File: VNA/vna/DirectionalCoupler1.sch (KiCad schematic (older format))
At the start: 4 parts, among them T1 1:10, T2 1:10

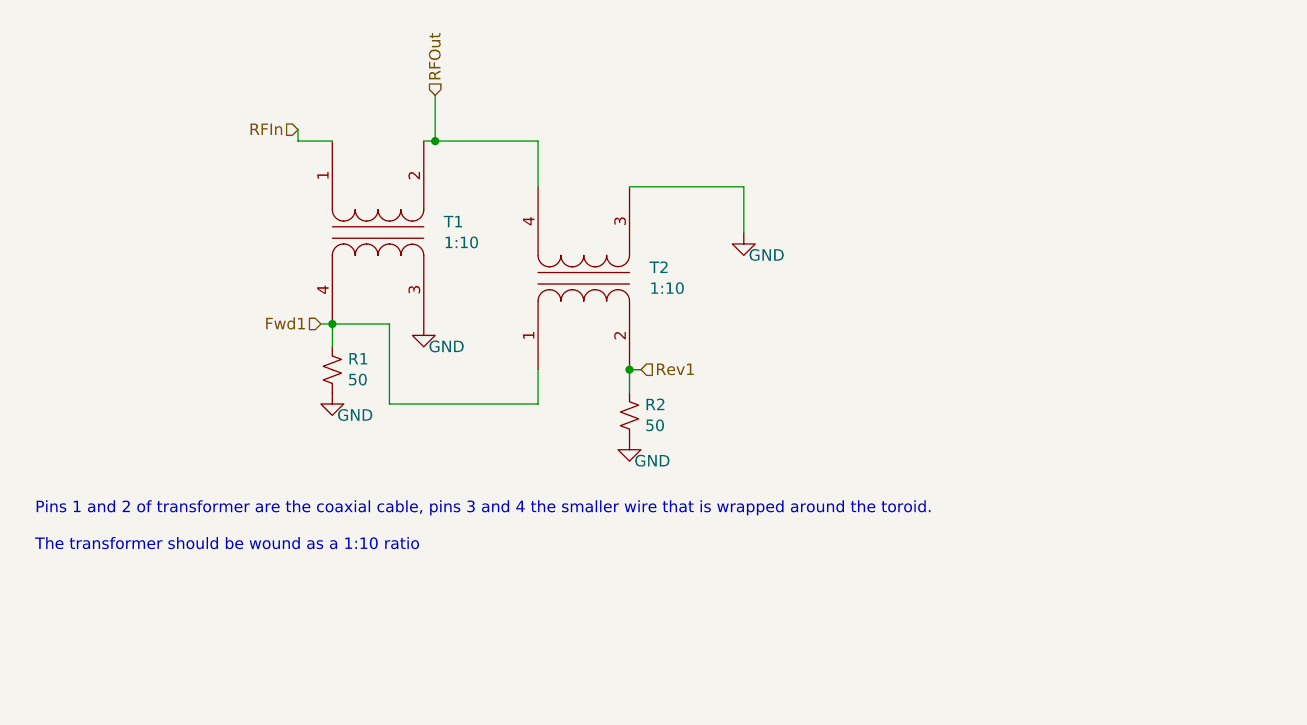
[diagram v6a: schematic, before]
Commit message: custom footprint for couplers, added decoupling caps
added custom footprint for directional couplers - will need to verify it

added decoupling caps to ad9851
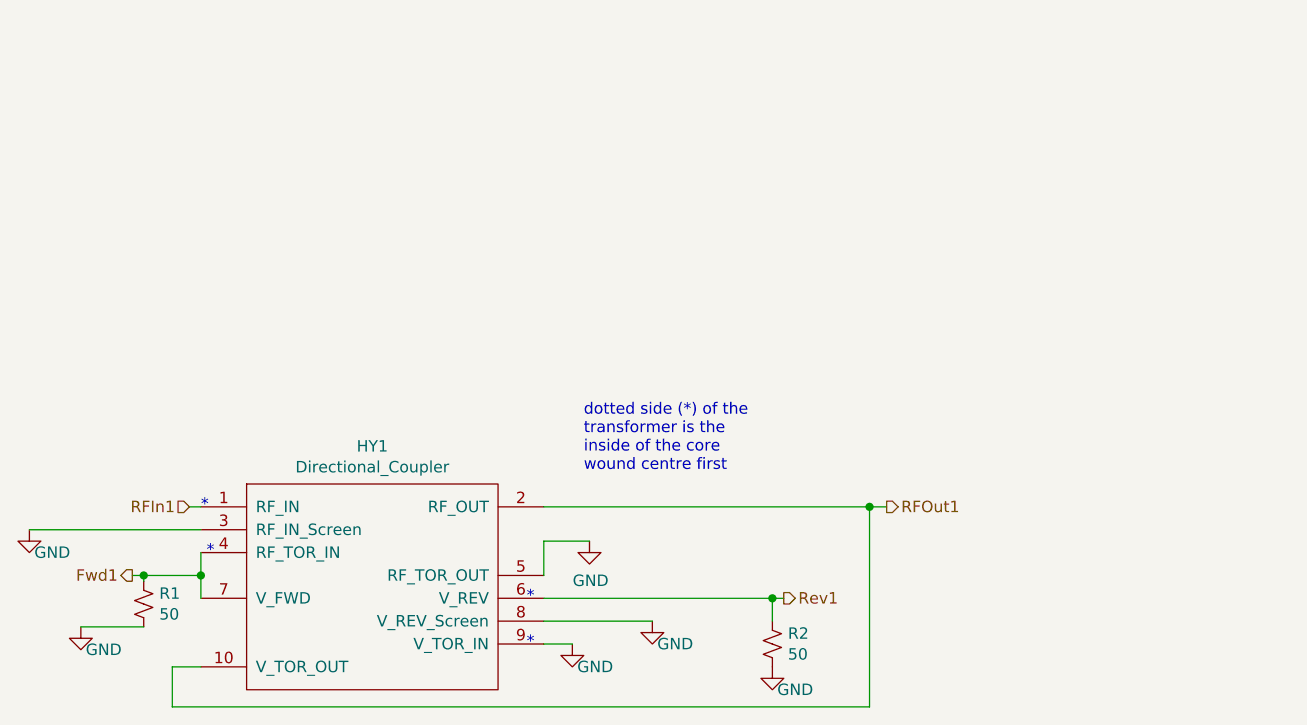
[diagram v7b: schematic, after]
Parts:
- removed T1, T2: 1:10, symbol Device:Transformer_1P_1S
- added HY1: Directional_Coupler, vna:Directional_Coupler, symbol vna-rescue:Directional_Coupler
- R1, R2: footprint Resistor_SMD:R_0805_2012Metric_Pad1.15x1.40mm_HandSolder -> Resistor_SMD:R_1206_3216Metric_Pad1.42x1.75mm_HandSolder
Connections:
- net Fwd1: now also HY1.4 (RF_TOR_IN), HY1.7 (V_FWD)
- net GND: now also HY1.3 (RF_IN_Screen), HY1.5 (RF_TOR_OUT), HY1.8 (V_REV_Screen), HY1.9 (V_TOR_IN)
- net Rev1: now also HY1.6 (V_REV)
- new net RFIn1: HY1.1 (RF_IN)
- new net RFOut1: HY1.10 (V_TOR_OUT), HY1.2 (RF_OUT)
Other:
- note added: "*"
- note added: "dotted side (*) of the \ntransformer is the \ninside of the core\nwound centre first"
- note removed: "Pins 1 and 2 of transformer are the coaxial cable, pins 3 and 4 the smaller wire that is wrapped around the toroid.\n\nThe transformer should be wound as a 1:10 ratio"
- moved on the sheet: R1, R2
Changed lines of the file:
@@
 Comment4 ""
 $EndDescr
-Wire Wire Line
-	6050 2300 6550 2300
-Wire Wire Line
-	6550 2300 6550 2500
 $Comp
 L power:GND #PWR08
 U 1 1 5CF4AF9A
-P 6550 2500
+P 6150 4200
 AR Path="/5CC1CC6B/5CF4AF9A" Ref="#PWR08"  Part="1"
 AR Path="/5CC2F156/5CF4AF9A" Ref="#PWR?"  Part="1"
 AR Path="/5CC6A089/5CF4AF9A" Ref="#PWR?"  Part="1"
-F 0 "#PWR08" H 6550 2250 50  0001 C CNN
-F 1 "GND" H 6650 2400 50  0000 C CNN
-F 2 "" H 6550 2500 50  0001 C CNN
-F 3 "" H 6550 2500 50  0001 C CNN
-	1    6550 2500
+F 0 "#PWR08" H 6150 3950 50  0001 C CNN
+F 1 "GND" H 6250 4100 50  0000 C CNN
+F 2 "" H 6150 4200 50  0001 C CNN
+F 3 "" H 6150 4200 50  0001 C CNN
+	1    6150 4200
 	1    0    0    -1
 $EndComp
@@
 L Device:R_Small_US R2
 U 1 1 5CF4AFA0
-P 6050 3300
+P 6675 4300
 AR Path="/5CC1CC6B/5CF4AFA0" Ref="R2"  Part="1"
 AR Path="/5CC2F156/5CF4AFA0" Ref="R?"  Part="1"
 AR Path="/5CC6A089/5CF4AFA0" Ref="R?"  Part="1"
-F 0 "R2" H 6118 3346 50  0000 L CNN
-F 1 "50" H 6118 3255 50  0000 L CNN
-F 2 "Resistor_SMD:R_0805_2012Metric_Pad1.15x1.40mm_HandSolder" H 6050 3300 50  0001 C CNN
-F 3 "~" H 6050 3300 50  0001 C CNN
-	1    6050 3300
+F 0 "R2" H 6743 4346 50  0000 L CNN
+F 1 "50" H 6743 4255 50  0000 L CNN
+F 2 "Resistor_SMD:R_1206_3216Metric_Pad1.42x1.75mm_HandSolder" H 6675 4300 50  0001 C CNN
+F 3 "~" H 6675 4300 50  0001 C CNN
+	1    6675 4300
 	1    0    0    -1
 $EndComp
@@
 L Device:R_Small_US R1
 U 1 1 5CF4AFA6
-P 4750 3100
+P 3925 4125
 AR Path="/5CC1CC6B/5CF4AFA6" Ref="R1"  Part="1"
 AR Path="/5CC2F156/5CF4AFA6" Ref="R?"  Part="1"
 AR Path="/5CC6A089/5CF4AFA6" Ref="R?"  Part="1"
-F 0 "R1" H 4818 3146 50  0000 L CNN
-F 1 "50" H 4818 3055 50  0000 L CNN
-F 2 "Resistor_SMD:R_0805_2012Metric_Pad1.15x1.40mm_HandSolder" H 4750 3100 50  0001 C CNN
-F 3 "~" H 4750 3100 50  0001 C CNN
-	1    4750 3100
+F 0 "R1" H 3993 4171 50  0000 L CNN
+F 1 "50" H 3993 4080 50  0000 L CNN
+F 2 "Resistor_SMD:R_1206_3216Metric_Pad1.42x1.75mm_HandSolder" H 3925 4125 50  0001 C CNN
+F 3 "~" H 3925 4125 50  0001 C CNN
+	1    3925 4125
 	1    0    0    -1
 $EndComp
 Wire Wire Line
-	4750 2900 4700 2900
+	6675 4100 6725 4100
 Wire Wire Line
-	4750 3000 4750 2900
-Wire Wire Line
-	6050 3100 6100 3100
-Wire Wire Line
-	6050 3200 6050 3100
+	6675 4200 6675 4100
 $Comp
 L power:GND #PWR010
 U 1 1 5CF4AFB0
-P 4750 3200
+P 3650 4225
 AR Path="/5CC1CC6B/5CF4AFB0" Ref="#PWR010"  Part="1"
 AR Path="/5CC2F156/5CF4AFB0" Ref="#PWR?"  Part="1"
 AR Path="/5CC6A089/5CF4AFB0" Ref="#PWR?"  Part="1"
-F 0 "#PWR010" H 4750 2950 50  0001 C CNN
-F 1 "GND" H 4850 3100 50  0000 C CNN
-F 2 "" H 4750 3200 50  0001 C CNN
-F 3 "" H 4750 3200 50  0001 C CNN
-	1    4750 3200
+F 0 "#PWR010" H 3650 3975 50  0001 C CNN
+F 1 "GND" H 3750 4125 50  0000 C CNN
+F 2 "" H 3650 4225 50  0001 C CNN
+F 3 "" H 3650 4225 50  0001 C CNN
+	1    3650 4225
 	1    0    0    -1
 $EndComp
@@
 L power:GND #PWR011
 U 1 1 5CF4AFB6
-P 6050 3400
+P 6675 4400
 AR Path="/5CC1CC6B/5CF4AFB6" Ref="#PWR011"  Part="1"
 AR Path="/5CC2F156/5CF4AFB6" Ref="#PWR?"  Part="1"
 AR Path="/5CC6A089/5CF4AFB6" Ref="#PWR?"  Part="1"
-F 0 "#PWR011" H 6050 3150 50  0001 C CNN
-F 1 "GND" H 6150 3300 50  0000 C CNN
-F 2 "" H 6050 3400 50  0001 C CNN
-F 3 "" H 6050 3400 50  0001 C CNN
-	1    6050 3400
+F 0 "#PWR011" H 6675 4150 50  0001 C CNN
+F 1 "GND" H 6775 4300 50  0000 C CNN
+F 2 "" H 6675 4400 50  0001 C CNN
+F 3 "" H 6675 4400 50  0001 C CNN
+	1    6675 4400
+	1    0    0    -1
+$EndComp
+Text HLabel 3875 4000 0    50   Output ~ 0
+Fwd1
+Text HLabel 6725 4100 2    50   Output ~ 0
+Rev1
+Text HLabel 7175 3700 2    50   Output ~ 0
+RFOut1
+Text HLabel 4125 3700 0    50   Input ~ 0
+RFIn1
+$Comp
+L power:GND #PWR09
+U 1 1 5CF4AFD9
+P 3425 3800
+AR Path="/5CC1CC6B/5CF4AFD9" Ref="#PWR09"  Part="1"
+AR Path="/5CC2F156/5CF4AFD9" Ref="#PWR?"  Part="1"
+AR Path="/5CC6A089/5CF4AFD9" Ref="#PWR?"  Part="1"
+F 0 "#PWR09" H 3425 3550 50  0001 C CNN
+F 1 "GND" H 3525 3700 50  0000 C CNN
+F 2 "" H 3425 3800 50  0001 C CNN
+F 3 "" H 3425 3800 50  0001 C CNN
+	1    3425 3800
+	1    0    0    -1
+$EndComp
+$Comp
+L vna-rescue:Directional_Coupler HY1
+U 1 1 5D92701E
+P 4925 4050
+F 0 "HY1" H 4925 4665 50  0000 C CNN
+F 1 "Directional_Coupler" H 4925 4574 50  0000 C CNN
+F 2 "vna:Directional_Coupler" H 6025 4000 50  0001 C CNN
+F 3 "" H 6025 4000 50  0001 C CNN
+	1    4925 4050
 	1    0    0    -1
 $EndComp
 Wire Wire Line
-	5200 2100 5200 1900
+	3425 3800 4175 3800
 Wire Wire Line
-	4750 2100 4600 2100
+	5675 4200 6150 4200
+Text Notes 5850 3550 0    50   ~ 0
+dotted side (*) of the \ntransformer is the \ninside of the core\nwound centre first
 Wire Wire Line
-	4600 2100 4600 2050
+	4175 3900 4175 4000
 Wire Wire Line
-	5650 2100 5650 2300
+	4175 4000 3925 4000
 Wire Wire Line
-	5150 2100 5200 2100
+	3925 4000 3925 4025
+Connection ~ 4175 4000
 Wire Wire Line
-	5200 2100 5650 2100
-Connection ~ 5200 2100
-Text HLabel 4700 2900 0    50   Input ~ 0
-Fwd1
-Text HLabel 6100 3100 2    50   Input ~ 0
-Rev1
-Text HLabel 5200 1900 1    50   Input ~ 0
-RFOut
-Text HLabel 4600 2050 0    50   Input ~ 0
-RFIn
+	4175 4000 4175 4100
+Wire Wire Line
+	3875 4000 3925 4000
+Connection ~ 3925 4000
+Wire Wire Line
+	4125 3700 4175 3700
+Wire Wire Line
+	3925 4225 3650 4225
 $Comp
-L Device:Transformer_1P_1S T1
-U 1 1 5CF4AFC7
-P 4950 2500
-F 0 "T1" V 4904 2212 50  0000 R CNN
-F 1 "1:10" V 4995 2212 50  0000 R CNN
-F 2 "" H 4950 2500 50  0001 C CNN
-F 3 "~" H 4950 2500 50  0001 C CNN
-	1    4950 2500
-	0    -1   1    0
-$EndComp
-$Comp
-L Device:Transformer_1P_1S T2
-U 1 1 5CF4AFCD
-P 5850 2700
-F 0 "T2" V 5896 2412 50  0000 R CNN
-F 1 "1:10" V 5805 2412 50  0000 R CNN
-F 2 "" H 5850 2700 50  0001 C CNN
-F 3 "~" H 5850 2700 50  0001 C CNN
-	1    5850 2700
-	0    -1   -1   0
-$EndComp
-Connection ~ 4750 2900
-Connection ~ 6050 3100
-Wire Wire Line
-	4750 2900 5000 2900
-Wire Wire Line
-	5000 2900 5000 3250
-Wire Wire Line
-	5000 3250 5650 3250
-Wire Wire Line
-	5650 3250 5650 3100
-$Comp
-L power:GND #PWR09
-U 1 1 5CF4AFD9
-P 5150 2900
-AR Path="/5CC1CC6B/5CF4AFD9" Ref="#PWR09"  Part="1"
-AR Path="/5CC2F156/5CF4AFD9" Ref="#PWR?"  Part="1"
-AR Path="/5CC6A089/5CF4AFD9" Ref="#PWR?"  Part="1"
-F 0 "#PWR09" H 5150 2650 50  0001 C CNN
-F 1 "GND" H 5250 2800 50  0000 C CNN
-F 2 "" H 5150 2900 50  0001 C CNN
-F 3 "" H 5150 2900 50  0001 C CNN
-	1    5150 2900
+L power:GND #PWR0105
+U 1 1 5D92D93C
+P 5800 4300
+AR Path="/5CC1CC6B/5D92D93C" Ref="#PWR0105"  Part="1"
+AR Path="/5CC2F156/5D92D93C" Ref="#PWR?"  Part="1"
+AR Path="/5CC6A089/5D92D93C" Ref="#PWR?"  Part="1"
+F 0 "#PWR0105" H 5800 4050 50  0001 C CNN
+F 1 "GND" H 5900 4200 50  0000 C CNN
+F 2 "" H 5800 4300 50  0001 C CNN
+F 3 "" H 5800 4300 50  0001 C CNN
+	1    5800 4300
 	1    0    0    -1
 $EndComp
-Text Notes 3450 3900 0    50   ~ 0
-Pins 1 and 2 of transformer are the coaxial cable, pins 3 and 4 the smaller wire that is wrapped around the toroid.\n\nThe transformer should be wound as a 1:10 ratio
+Wire Wire Line
+	4050 4400 4175 4400
+Wire Wire Line
+	5675 4100 6675 4100
+Connection ~ 6675 4100
+Wire Wire Line
+	7100 4575 7100 3700
+Wire Wire Line
+	5675 3700 7100 3700
+Wire Wire Line
+	7100 3700 7175 3700
+Connection ~ 7100 3700
+$Comp
+L power:GND #PWR0106
+U 1 1 5D9340D4
+P 5875 3850
+F 0 "#PWR0106" H 5875 3600 50  0001 C CNN
+F 1 "GND" H 5880 3677 50  0000 C CNN
+F 2 "" H 5875 3850 50  0001 C CNN
+F 3 "" H 5875 3850 50  0001 C CNN
+	1    5875 3850
+	1    0    0    -1
+$EndComp
+Wire Wire Line
+	5675 4000 5675 3850
+Wire Wire Line
+	5675 3850 5875 3850
+Wire Wire Line
+	5675 4300 5800 4300
+Wire Wire Line
+	4050 4400 4050 4575
+Wire Wire Line
+	4050 4575 7100 4575
+Text Notes 4175 3725 0    50   ~ 0
+*
+Text Notes 4200 3925 0    50   ~ 0
+*
+Text Notes 5600 4125 0    50   ~ 0
+*
+Text Notes 5600 4325 0    50   ~ 0
+*
 $EndSCHEMATC

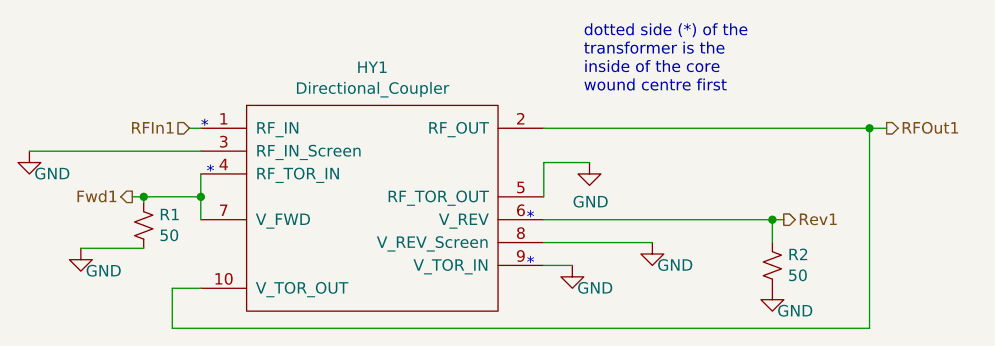
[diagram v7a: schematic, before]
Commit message: initial pcb design
initial layout and grouping of components complete
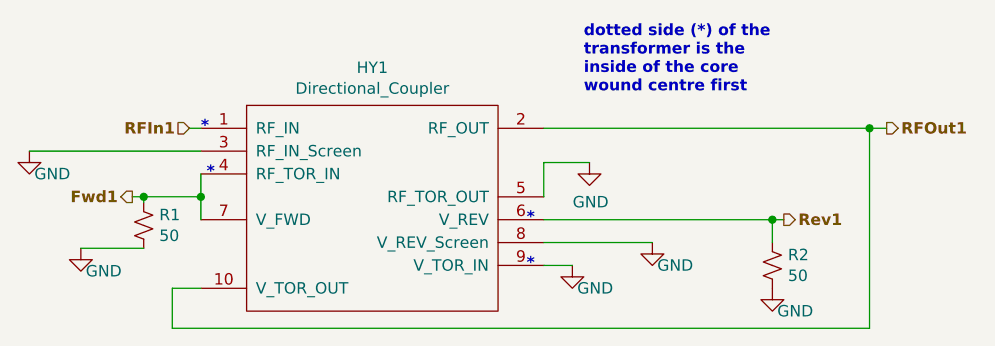
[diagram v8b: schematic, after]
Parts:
- R1, R2: footprint Resistor_SMD:R_1206_3216Metric_Pad1.42x1.75mm_HandSolder -> Resistor_SMD:R_0805_2012Metric_Pad1.15x1.40mm_HandSolder
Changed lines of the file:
@@
 encoding utf-8
 Sheet 2 10
-Title ""
+Title "Directional Coupler 1"
 Date ""
-Rev ""
-Comp ""
+Rev "0.1"
+Comp "Benjamin Jackson"
 Comment1 ""
 Comment2 ""
@@
 F 0 "R2" H 6743 4346 50  0000 L CNN
 F 1 "50" H 6743 4255 50  0000 L CNN
-F 2 "Resistor_SMD:R_1206_3216Metric_Pad1.42x1.75mm_HandSolder" H 6675 4300 50  0001 C CNN
+F 2 "Resistor_SMD:R_0805_2012Metric_Pad1.15x1.40mm_HandSolder" H 6675 4300 50  0001 C CNN
 F 3 "~" H 6675 4300 50  0001 C CNN
 	1    6675 4300
@@
 F 0 "R1" H 3993 4171 50  0000 L CNN
 F 1 "50" H 3993 4080 50  0000 L CNN
-F 2 "Resistor_SMD:R_1206_3216Metric_Pad1.42x1.75mm_HandSolder" H 3925 4125 50  0001 C CNN
+F 2 "Resistor_SMD:R_0805_2012Metric_Pad1.15x1.40mm_HandSolder" H 3925 4125 50  0001 C CNN
 F 3 "~" H 3925 4125 50  0001 C CNN
 	1    3925 4125
@@
 	1    0    0    -1
 $EndComp
-Text HLabel 3875 4000 0    50   Output ~ 0
+Text HLabel 3875 4000 0    50   Output ~ 10
 Fwd1
-Text HLabel 6725 4100 2    50   Output ~ 0
+Text HLabel 6725 4100 2    50   Output ~ 10
 Rev1
-Text HLabel 7175 3700 2    50   Output ~ 0
+Text HLabel 7175 3700 2    50   Output ~ 10
 RFOut1
-Text HLabel 4125 3700 0    50   Input ~ 0
+Text HLabel 4125 3700 0    50   Input ~ 10
 RFIn1
 $Comp
@@
 Wire Wire Line
 	5675 4200 6150 4200
-Text Notes 5850 3550 0    50   ~ 0
+Text Notes 5850 3550 0    50   ~ 10
 dotted side (*) of the \ntransformer is the \ninside of the core\nwound centre first
 Wire Wire Line
@@
 Wire Wire Line
 	4050 4575 7100 4575
-Text Notes 4175 3725 0    50   ~ 0
+Text Notes 4175 3725 0    50   ~ 10
 *
-Text Notes 4200 3925 0    50   ~ 0
+Text Notes 4200 3925 0    50   ~ 10
 *
-Text Notes 5600 4125 0    50   ~ 0
+Text Notes 5600 4125 0    50   ~ 10
 *
-Text Notes 5600 4325 0    50   ~ 0
+Text Notes 5600 4325 0    50   ~ 10
 *
 $EndSCHEMATC
